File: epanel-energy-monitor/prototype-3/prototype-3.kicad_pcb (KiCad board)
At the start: 2 copper layers, 100 x 100 mm, 68 parts, among them J1 Conn_01x01_Male, J10 Conn_01x03_Male, J11 Conn_01x03_Male, J12 Conn_01x03_Male, J13 Conn_01x03_Male, J14 Conn_02x05, J15 Conn_02x05, J16 Conn_02x05, J17 Screw_Terminal_01x02, J18 Screw_Terminal_01x02, J19 Screw_Terminal_01x02, J2 Conn_01x01_Male, J3 Screw_Terminal_01x02, J4 Conn_01x01, J5 Screw_Terminal_01x02, J6 Conn_02x03, J7 Conn_02x03, J8 Conn_02x03, J9 Conn_02x03, Q1 BSS138, T1 230V - 6V, U1 ESP32-POE, U2 LTV-814, U3 MCP3208, U4 ADS1115, U5 LMV321

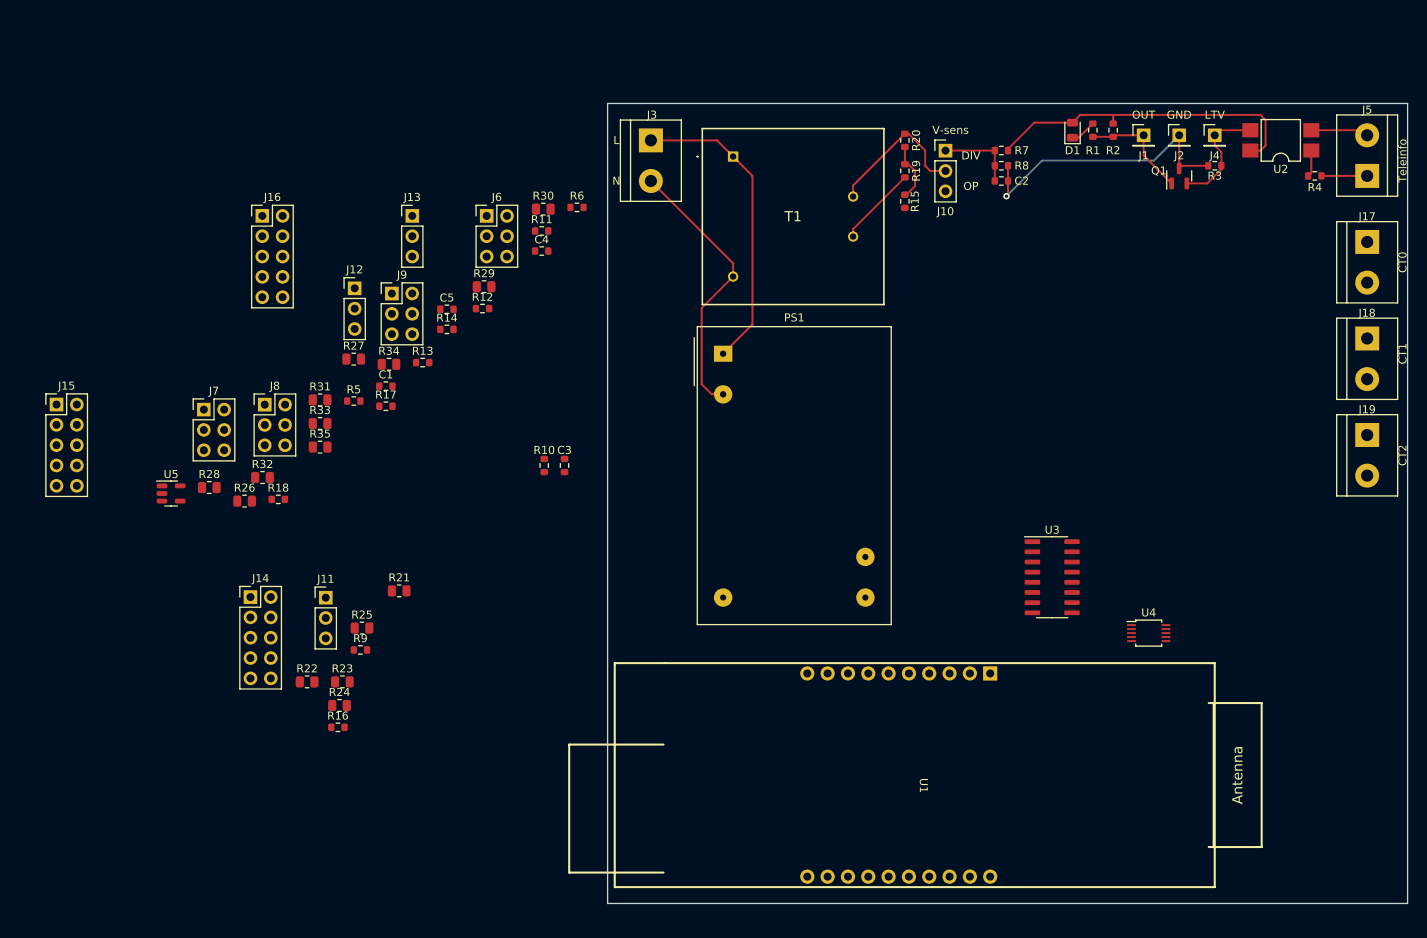
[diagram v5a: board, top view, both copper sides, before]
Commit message: more sensors
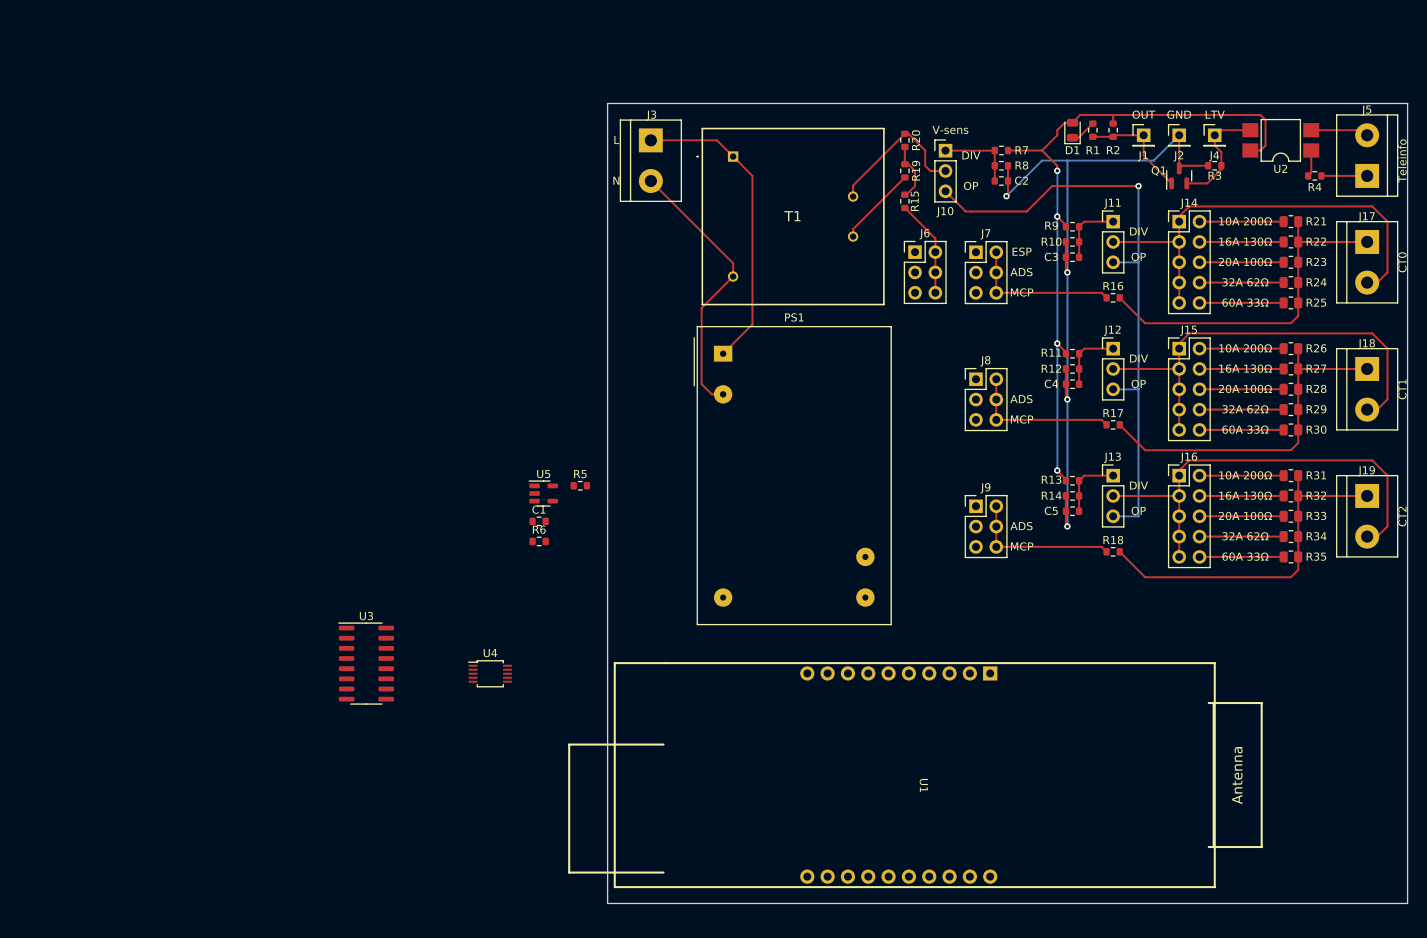
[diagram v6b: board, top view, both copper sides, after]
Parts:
- moved J15 140.5 mm to (171.4, 80.6)
- moved R28 135.8 mm to (185.4, 85.7), turned to 180 degrees
- moved R22 134.7 mm to (185.4, 67.3), turned to 180 degrees
- moved R26 132.2 mm to (185.4, 80.6), turned to 180 degrees
- moved R24 130.1 mm to (185.4, 72.4), turned to 180 degrees
- moved R23 129.7 mm to (185.4, 69.8), turned to 180 degrees
- moved R32 128.6 mm to (185.4, 99.1), turned to 180 degrees
- moved J14 125.2 mm to (171.4, 64.8)
- moved R25 123.0 mm to (185.4, 74.9), turned to 180 degrees
- moved R35 122.1 mm to (185.4, 106.7), turned to 180 degrees
- moved R33 121.9 mm to (185.4, 101.6), turned to 180 degrees
- moved R31 121.7 mm to (185.4, 96.5), turned to 180 degrees
- moved R21 120.6 mm to (185.4, 64.8), turned to 180 degrees
- moved J16 119.1 mm to (171.4, 96.5)
- moved R27 117.2 mm to (185.4, 83.2), turned to 180 degrees
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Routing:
- net Net-(J10-Pad3): track 0.00 -> 77.3 mm, vias 0 -> 1
- net GND: track 36.5 -> 93.9 mm, vias 1 -> 4
- net Net-(J13-Pad2): track 0.00 -> 55.8 mm
- net Net-(J12-Pad2): track 0.00 -> 55.8 mm
- net Net-(J11-Pad2): track 0.00 -> 55.8 mm
- net +3V3: track 40.8 -> 87.0 mm, vias 0 -> 4
- net Net-(J19-Pad1): track 0.00 -> 44.4 mm
- net Net-(J18-Pad1): track 0.00 -> 44.4 mm
- net Net-(J17-Pad1): track 0.00 -> 44.4 mm
- net Net-(J9-Pad2): track 0.00 -> 19.1 mm
- net Net-(J8-Pad2): track 0.00 -> 19.1 mm
- net Net-(J7-Pad2): track 0.00 -> 19.1 mm
- net Net-(J6-Pad2): track 0.00 -> 12.2 mm
- net Net-(J16-Pad8): track 0.00 -> 10.5 mm
- net Net-(J16-Pad6): track 0.00 -> 10.5 mm
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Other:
- board text added: "10A 200Ω"
- board text added: "16A 130Ω"
- board text added: "20A 100Ω"
- board text added: "32A 62Ω"
- board text added: "60A 33Ω"
- board text added: "ADS"
- board text added: "ESP"
- board text added: "MCP"

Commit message: add ampli op
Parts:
- moved C1 72.4 mm to (162.8, 114.9)
- moved R6 71.8 mm to (162.8, 113.0), turned to 180 degrees
- moved U5 68.4 mm to (158.9, 113.0), turned to -90 degrees
- moved R5 67.5 mm to (162.8, 111.1)
- moved U3 50.4 mm to (118.7, 132.1)
- moved U4 44.3 mm to (128.9, 129.5)
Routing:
- net +3V3: track 87.0 -> 125.1 mm, vias 4 -> 5
- net GND: track 93.9 -> 116.6 mm, vias 4 -> 6
- net Net-(J10-Pad3): track 77.3 -> 91.3 mm, vias 1 -> 2
- net Net-(C1-Pad1): track 0.00 -> 5.87 mm

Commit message: wip
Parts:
- moved U3 27.9 mm to (146.7, 131.4)
- moved U4 26.7 mm to (155.6, 128.3)
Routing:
- net Net-(J7-Pad1): track 0.00 -> 107.1 mm
- net Net-(J6-Pad1): track 0.00 -> 96.8 mm
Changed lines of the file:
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@@
   )
   (footprint "Package_SO:SOIC-16_3.9x9.9mm_P1.27mm" (layer "F.Cu")
-    (at 118.745 132.08)
+    (at 146.685 131.445)
     (descr "SOIC, 16 Pin (JEDEC MS-012AC, https://www.analog.com/media/en/package-pcb-resources/package/pkg_pdf/soic_narrow-r/r_16.pdf), generated with kicad-footprint-generator ipc_gullwing_generator.py")
     (tags "SOIC SO")
@@
   )
   (footprint "Package_SO:TSSOP-10_3x3mm_P0.5mm" (layer "F.Cu")
-    (at 128.905 129.54)
+    (at 155.575 128.27)
     (descr "TSSOP10: plastic thin shrink small outline package; 10 leads; body width 3 mm; (see NXP SSOP-TSSOP-VSO-REFLOW.pdf and sot552-1_po.pdf)")
     (tags "SSOP 0.5")
@@
   (segment (start 158.94 100.965) (end 158.94 99.06) (width 0.25) (layer "F.Cu") (net 8))
   (segment (start 158.94 99.06) (end 158.94 97.155) (width 0.25) (layer "F.Cu") (net 8))
+  (segment (start 135.125 145.285) (end 117.475 127.635) (width 0.25) (layer "B.Cu") (net 9))
+  (segment (start 117.475 127.635) (end 117.475 84.455) (width 0.25) (layer "B.Cu") (net 9))
+  (segment (start 135.89 66.04) (end 144.145 66.04) (width 0.25) (layer "B.Cu") (net 9))
+  (segment (start 117.475 84.455) (end 135.89 66.04) (width 0.25) (layer "B.Cu") (net 9))
+  (segment (start 146.045 67.94) (end 146.045 68.595) (width 0.25) (layer "B.Cu") (net 9))
+  (segment (start 135.125 146.645) (end 135.125 145.285) (width 0.25) (layer "B.Cu") (net 9))
+  (segment (start 144.145 66.04) (end 146.045 67.94) (width 0.25) (layer "B.Cu") (net 9))
   (segment (start 118.11 77.6125) (end 118.11 59.055) (width 0.25) (layer "F.Cu") (net 10))
   (segment (start 118.11 59.055) (end 115.69 56.635) (width 0.25) (layer "F.Cu") (net 10))
@@
   (segment (start 187.96 53.34) (end 194.31 53.34) (width 0.25) (layer "F.Cu") (net 18))
   (segment (start 194.31 53.34) (end 194.945 53.975) (width 0.25) (layer "F.Cu") (net 18))
+  (segment (start 118.11 85.09) (end 118.11 127.09) (width 0.25) (layer "B.Cu") (net 19))
+  (segment (start 118.11 127.09) (end 137.665 146.645) (width 0.25) (layer "B.Cu") (net 19))
+  (segment (start 138.43 68.58) (end 134.62 68.58) (width 0.25) (layer "B.Cu") (net 19))
+  (segment (start 134.62 68.58) (end 118.11 85.09) (width 0.25) (layer "B.Cu") (net 19))
   (segment (start 137.16 63.055) (end 140.97 66.865) (width 0.25) (layer "F.Cu") (net 28))
   (segment (start 140.97 73.66) (end 140.97 71.12) (width 0.25) (layer "F.Cu") (net 28))
